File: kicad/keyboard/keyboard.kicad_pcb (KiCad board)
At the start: 2 copper layers, 16 parts, among them P1 CONN03, P2 CONN06, P3 CONN12, P4 CONN16, U1 atmega328, U2 MAX7219, Y1 Crystal

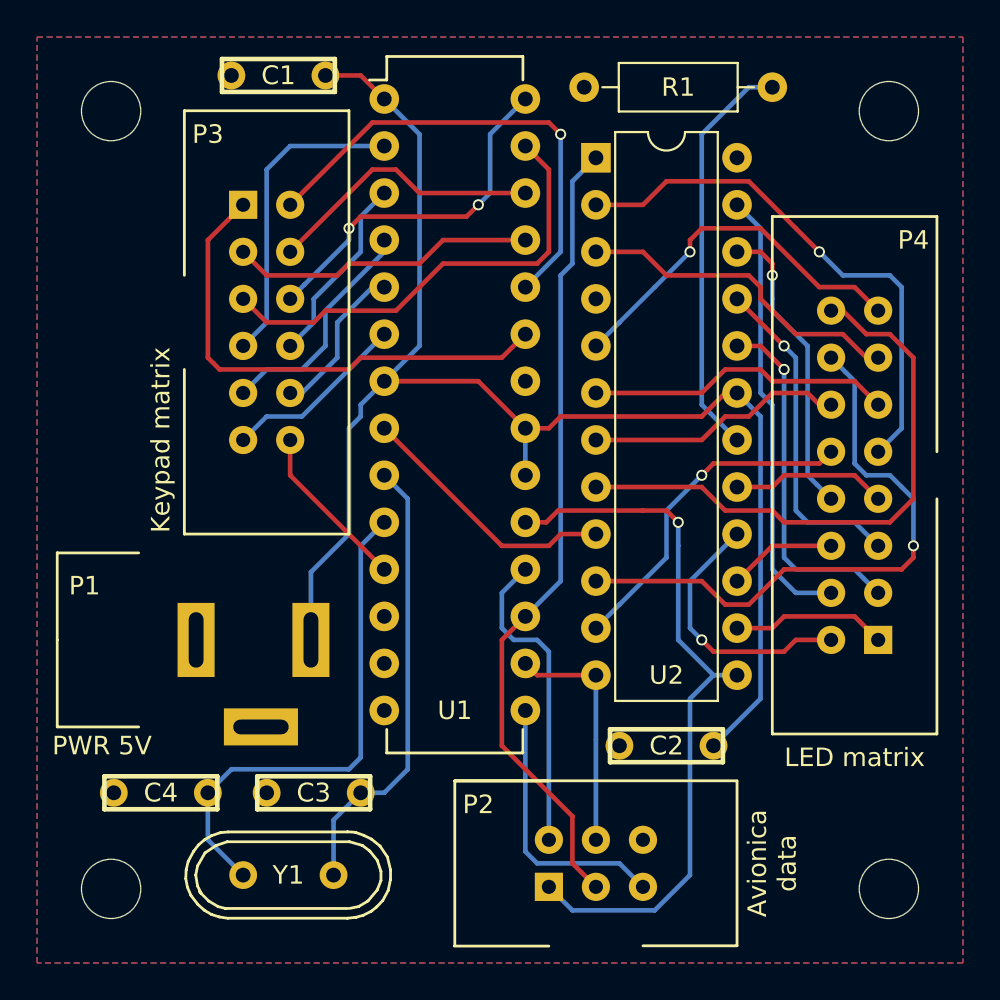
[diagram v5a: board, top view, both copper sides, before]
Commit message: Add a status LED to the Keypad Controller board
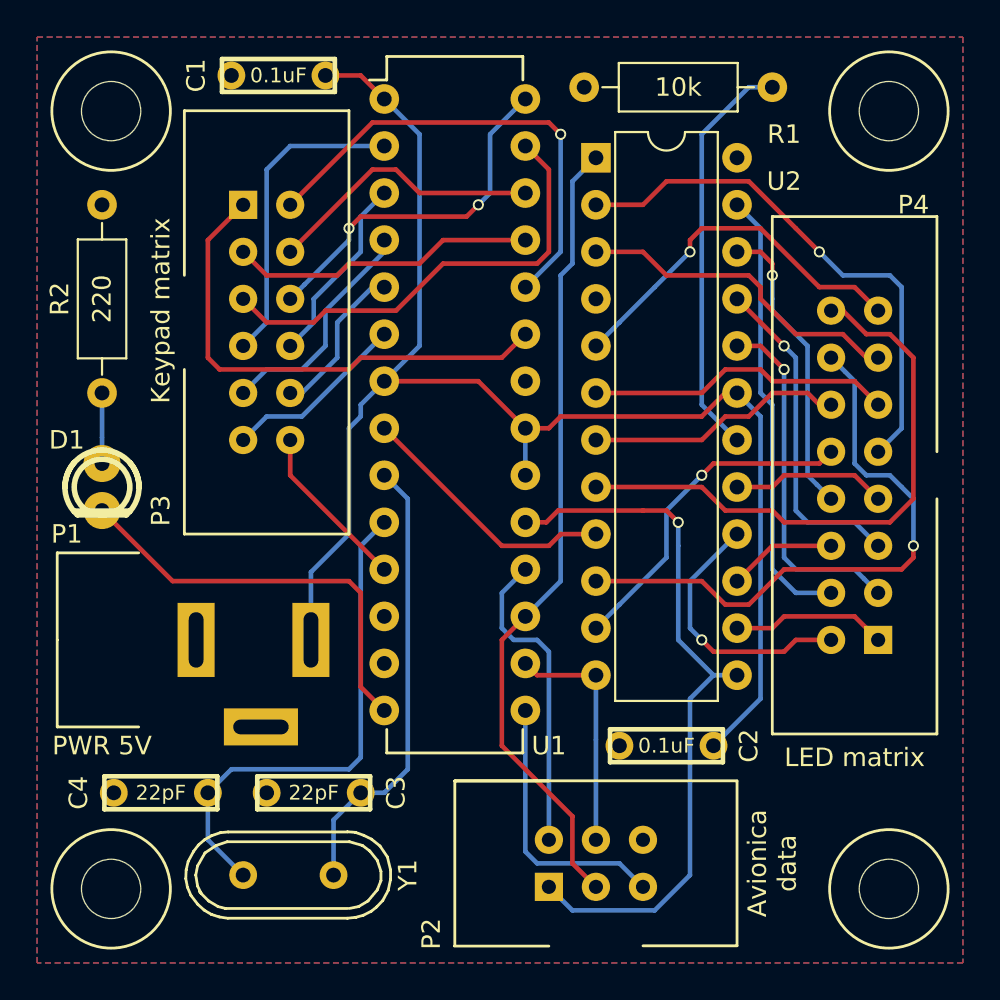
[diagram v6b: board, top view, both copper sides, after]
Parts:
- added D1: LED, avionica:LED-th, F.Cu at (143.5, 114.3)
- added R2: 220, avionica:Axial_resistor, F.Cu at (143.5, 109.2)
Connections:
- U1 pad 14: (no net) -> Net-(D1-Pad2)
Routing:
- net Net-(D1-Pad2): track 0.00 -> 22.7 mm
- net Net-(D1-Pad1): track 0.00 -> 3.81 mm
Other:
- board text added: "Avionica Keypad Controller Board Rev01 Copyright (c) 2017 Alvaro Polo"
